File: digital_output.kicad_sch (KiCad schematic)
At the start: 12 parts, among them Q1 AOSP21321, Q2 AOSP21321, Q3 NMOS, Q4 NMOS

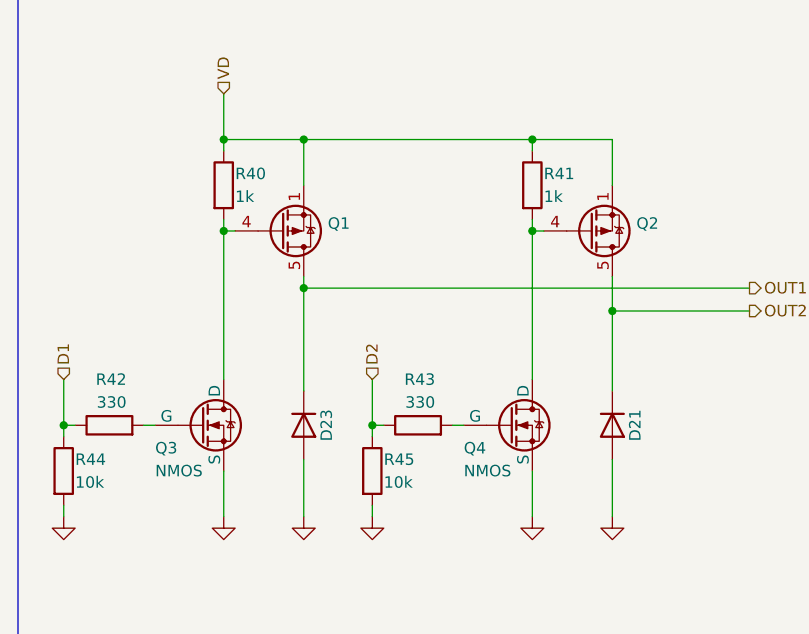
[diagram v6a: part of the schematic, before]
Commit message: fixed usb, added footprints
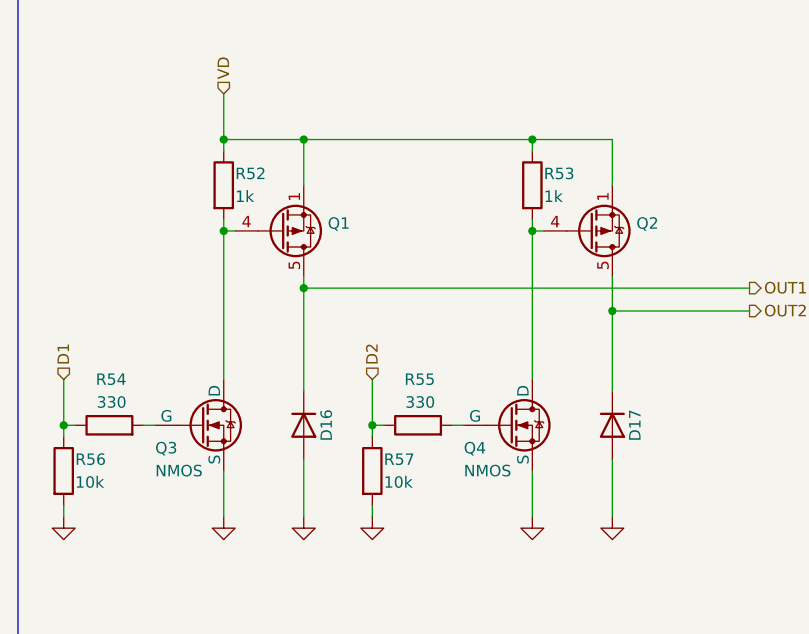
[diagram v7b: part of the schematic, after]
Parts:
- renumbered D23 to D16, D21 to D17, R40 to R52, R41 to R53, R42 to R54, R43 to R55, R44 to R56, R45 to R57
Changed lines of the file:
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@@
 		(on_board yes)
 		(dnp no)
-		(property "Reference" "R44"
+		(property "Reference" "R56"
 			(at 20.32 92.71 0)
 			(effects
@@
 			(project "frodo_io_module"
 				(path "/c1ccca3c-4648-4b8e-86a1-690c24c5f13e/0f95e9ba-a3b8-427d-95e8-5ddc0cb3ef54"
-					(reference "R50")
-					(unit 1)
-				)
-				(path "/c1ccca3c-4648-4b8e-86a1-690c24c5f13e/1daa12b0-ccec-42a7-b3b8-2333aafbd367"
-					(reference "R44")
+					(reference "R62")
+					(unit 1)
+				)
+				(path "/c1ccca3c-4648-4b8e-86a1-690c24c5f13e/1daa12b0-ccec-42a7-b3b8-2333aafbd367"
+					(reference "R56")
 					(unit 1)
 				)
@@
 		(on_board yes)
 		(dnp no)
-		(property "Reference" "R41"
+		(property "Reference" "R53"
 			(at 72.39 60.96 0)
 			(effects
@@
 			(project "frodo_io_module"
 				(path "/c1ccca3c-4648-4b8e-86a1-690c24c5f13e/0f95e9ba-a3b8-427d-95e8-5ddc0cb3ef54"
-					(reference "R47")
-					(unit 1)
-				)
-				(path "/c1ccca3c-4648-4b8e-86a1-690c24c5f13e/1daa12b0-ccec-42a7-b3b8-2333aafbd367"
-					(reference "R41")
+					(reference "R59")
+					(unit 1)
+				)
+				(path "/c1ccca3c-4648-4b8e-86a1-690c24c5f13e/1daa12b0-ccec-42a7-b3b8-2333aafbd367"
+					(reference "R53")
 					(unit 1)
 				)
@@
 		(on_board yes)
 		(dnp no)
-		(property "Reference" "D21"
+		(property "Reference" "D17"
 			(at 82.55 88.9 0)
 			(effects
@@
 			(project "frodo_io_module"
 				(path "/c1ccca3c-4648-4b8e-86a1-690c24c5f13e/0f95e9ba-a3b8-427d-95e8-5ddc0cb3ef54"
-					(reference "D22")
-					(unit 1)
-				)
-				(path "/c1ccca3c-4648-4b8e-86a1-690c24c5f13e/1daa12b0-ccec-42a7-b3b8-2333aafbd367"
-					(reference "D21")
+					(reference "D19")
+					(unit 1)
+				)
+				(path "/c1ccca3c-4648-4b8e-86a1-690c24c5f13e/1daa12b0-ccec-42a7-b3b8-2333aafbd367"
+					(reference "D17")
 					(unit 1)
 				)
@@
 		(on_board yes)
 		(dnp no)
-		(property "Reference" "R40"
+		(property "Reference" "R52"
 			(at 38.1 60.96 0)
 			(effects
@@
 			(project "frodo_io_module"
 				(path "/c1ccca3c-4648-4b8e-86a1-690c24c5f13e/0f95e9ba-a3b8-427d-95e8-5ddc0cb3ef54"
-					(reference "R46")
-					(unit 1)
-				)
-				(path "/c1ccca3c-4648-4b8e-86a1-690c24c5f13e/1daa12b0-ccec-42a7-b3b8-2333aafbd367"
-					(reference "R40")
+					(reference "R58")
+					(unit 1)
+				)
+				(path "/c1ccca3c-4648-4b8e-86a1-690c24c5f13e/1daa12b0-ccec-42a7-b3b8-2333aafbd367"
+					(reference "R52")
 					(unit 1)
 				)
@@
 		(dnp no)
 		(fields_autoplaced yes)
-		(property "Reference" "#PWR0116"
+		(property "Reference" "#PWR0122"
 			(at 36.83 105.41 0)
 			(effects
@@
 			(project "frodo_io_module"
 				(path "/c1ccca3c-4648-4b8e-86a1-690c24c5f13e/0f95e9ba-a3b8-427d-95e8-5ddc0cb3ef54"
+					(reference "#PWR0128")
+					(unit 1)
+				)
+				(path "/c1ccca3c-4648-4b8e-86a1-690c24c5f13e/1daa12b0-ccec-42a7-b3b8-2333aafbd367"
 					(reference "#PWR0122")
-					(unit 1)
-				)
-				(path "/c1ccca3c-4648-4b8e-86a1-690c24c5f13e/1daa12b0-ccec-42a7-b3b8-2333aafbd367"
-					(reference "#PWR0116")
 					(unit 1)
 				)
@@
 		(on_board yes)
 		(dnp no)
-		(property "Reference" "R42"
+		(property "Reference" "R54"
 			(at 26.035 83.82 90)
 			(effects
@@
 			(project "frodo_io_module"
 				(path "/c1ccca3c-4648-4b8e-86a1-690c24c5f13e/0f95e9ba-a3b8-427d-95e8-5ddc0cb3ef54"
-					(reference "R48")
-					(unit 1)
-				)
-				(path "/c1ccca3c-4648-4b8e-86a1-690c24c5f13e/1daa12b0-ccec-42a7-b3b8-2333aafbd367"
-					(reference "R42")
+					(reference "R60")
+					(unit 1)
+				)
+				(path "/c1ccca3c-4648-4b8e-86a1-690c24c5f13e/1daa12b0-ccec-42a7-b3b8-2333aafbd367"
+					(reference "R54")
 					(unit 1)
 				)
@@
 		(on_board yes)
 		(dnp no)
-		(property "Reference" "D23"
+		(property "Reference" "D16"
 			(at 48.26 88.9 0)
 			(effects
@@
 			(project "frodo_io_module"
 				(path "/c1ccca3c-4648-4b8e-86a1-690c24c5f13e/0f95e9ba-a3b8-427d-95e8-5ddc0cb3ef54"
-					(reference "D24")
-					(unit 1)
-				)
-				(path "/c1ccca3c-4648-4b8e-86a1-690c24c5f13e/1daa12b0-ccec-42a7-b3b8-2333aafbd367"
-					(reference "D23")
+					(reference "D18")
+					(unit 1)
+				)
+				(path "/c1ccca3c-4648-4b8e-86a1-690c24c5f13e/1daa12b0-ccec-42a7-b3b8-2333aafbd367"
+					(reference "D16")
 					(unit 1)
 				)
@@
 		(dnp no)
 		(fields_autoplaced yes)
-		(property "Reference" "#PWR0120"
+		(property "Reference" "#PWR0126"
 			(at 80.01 105.41 0)
 			(effects
@@
 			(project "frodo_io_module"
 				(path "/c1ccca3c-4648-4b8e-86a1-690c24c5f13e/0f95e9ba-a3b8-427d-95e8-5ddc0cb3ef54"
+					(reference "#PWR0132")
+					(unit 1)
+				)
+				(path "/c1ccca3c-4648-4b8e-86a1-690c24c5f13e/1daa12b0-ccec-42a7-b3b8-2333aafbd367"
 					(reference "#PWR0126")
-					(unit 1)
-				)
-				(path "/c1ccca3c-4648-4b8e-86a1-690c24c5f13e/1daa12b0-ccec-42a7-b3b8-2333aafbd367"
-					(reference "#PWR0120")
 					(unit 1)
 				)
@@
 		(dnp no)
 		(fields_autoplaced yes)
-		(property "Reference" "#PWR0115"
+		(property "Reference" "#PWR0121"
 			(at 19.05 105.41 0)
 			(effects
@@
 			(project "frodo_io_module"
 				(path "/c1ccca3c-4648-4b8e-86a1-690c24c5f13e/0f95e9ba-a3b8-427d-95e8-5ddc0cb3ef54"
+					(reference "#PWR0127")
+					(unit 1)
+				)
+				(path "/c1ccca3c-4648-4b8e-86a1-690c24c5f13e/1daa12b0-ccec-42a7-b3b8-2333aafbd367"
 					(reference "#PWR0121")
-					(unit 1)
-				)
-				(path "/c1ccca3c-4648-4b8e-86a1-690c24c5f13e/1daa12b0-ccec-42a7-b3b8-2333aafbd367"
-					(reference "#PWR0115")
 					(unit 1)
 				)
@@
 		(dnp no)
 		(fields_autoplaced yes)
-		(property "Reference" "#PWR0118"
+		(property "Reference" "#PWR0124"
 			(at 53.34 105.41 0)
 			(effects
@@
 			(project "frodo_io_module"
 				(path "/c1ccca3c-4648-4b8e-86a1-690c24c5f13e/0f95e9ba-a3b8-427d-95e8-5ddc0cb3ef54"
+					(reference "#PWR0130")
+					(unit 1)
+				)
+				(path "/c1ccca3c-4648-4b8e-86a1-690c24c5f13e/1daa12b0-ccec-42a7-b3b8-2333aafbd367"
 					(reference "#PWR0124")
-					(unit 1)
-				)
-				(path "/c1ccca3c-4648-4b8e-86a1-690c24c5f13e/1daa12b0-ccec-42a7-b3b8-2333aafbd367"
-					(reference "#PWR0118")
 					(unit 1)
 				)
@@
 		(on_board yes)
 		(dnp no)
-		(property "Reference" "R43"
+		(property "Reference" "R55"
 			(at 60.325 83.82 90)
 			(effects
@@
 			(project "frodo_io_module"
 				(path "/c1ccca3c-4648-4b8e-86a1-690c24c5f13e/0f95e9ba-a3b8-427d-95e8-5ddc0cb3ef54"
-					(reference "R49")
-					(unit 1)
-				)
-				(path "/c1ccca3c-4648-4b8e-86a1-690c24c5f13e/1daa12b0-ccec-42a7-b3b8-2333aafbd367"
-					(reference "R43")
+					(reference "R61")
+					(unit 1)
+				)
+				(path "/c1ccca3c-4648-4b8e-86a1-690c24c5f13e/1daa12b0-ccec-42a7-b3b8-2333aafbd367"
+					(reference "R55")
 					(unit 1)
 				)
@@
 		(dnp no)
 		(fields_autoplaced yes)
-		(property "Reference" "#PWR0119"
+		(property "Reference" "#PWR0125"
 			(at 71.12 105.41 0)
 			(effects
@@
 			(project "frodo_io_module"
 				(path "/c1ccca3c-4648-4b8e-86a1-690c24c5f13e/0f95e9ba-a3b8-427d-95e8-5ddc0cb3ef54"
+					(reference "#PWR0131")
+					(unit 1)
+				)
+				(path "/c1ccca3c-4648-4b8e-86a1-690c24c5f13e/1daa12b0-ccec-42a7-b3b8-2333aafbd367"
 					(reference "#PWR0125")
-					(unit 1)
-				)
-				(path "/c1ccca3c-4648-4b8e-86a1-690c24c5f13e/1daa12b0-ccec-42a7-b3b8-2333aafbd367"
-					(reference "#PWR0119")
 					(unit 1)
 				)
@@
 		(on_board yes)
 		(dnp no)
-		(property "Reference" "R45"
+		(property "Reference" "R57"
 			(at 54.61 92.71 0)
 			(effects
@@
 			(project "frodo_io_module"
 				(path "/c1ccca3c-4648-4b8e-86a1-690c24c5f13e/0f95e9ba-a3b8-427d-95e8-5ddc0cb3ef54"
-					(reference "R51")
-					(unit 1)
-				)
-				(path "/c1ccca3c-4648-4b8e-86a1-690c24c5f13e/1daa12b0-ccec-42a7-b3b8-2333aafbd367"
-					(reference "R45")
+					(reference "R63")
+					(unit 1)
+				)
+				(path "/c1ccca3c-4648-4b8e-86a1-690c24c5f13e/1daa12b0-ccec-42a7-b3b8-2333aafbd367"
+					(reference "R57")
 					(unit 1)
 				)
@@
 		(dnp no)
 		(fields_autoplaced yes)
-		(property "Reference" "#PWR0117"
+		(property "Reference" "#PWR0123"
 			(at 45.72 105.41 0)
 			(effects
@@
 			(project "frodo_io_module"
 				(path "/c1ccca3c-4648-4b8e-86a1-690c24c5f13e/0f95e9ba-a3b8-427d-95e8-5ddc0cb3ef54"
+					(reference "#PWR0129")
+					(unit 1)
+				)
+				(path "/c1ccca3c-4648-4b8e-86a1-690c24c5f13e/1daa12b0-ccec-42a7-b3b8-2333aafbd367"
 					(reference "#PWR0123")
 					(unit 1)
 				)
-				(path "/c1ccca3c-4648-4b8e-86a1-690c24c5f13e/1daa12b0-ccec-42a7-b3b8-2333aafbd367"
-					(reference "#PWR0117")
-					(unit 1)
-				)
